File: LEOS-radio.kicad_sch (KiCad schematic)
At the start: 19 parts, among them J1 MicroFit_1x4, J2 MicroFit_1x4, U1 MCP2562FD, U2 MCP2518FD, Y1 40 MHz

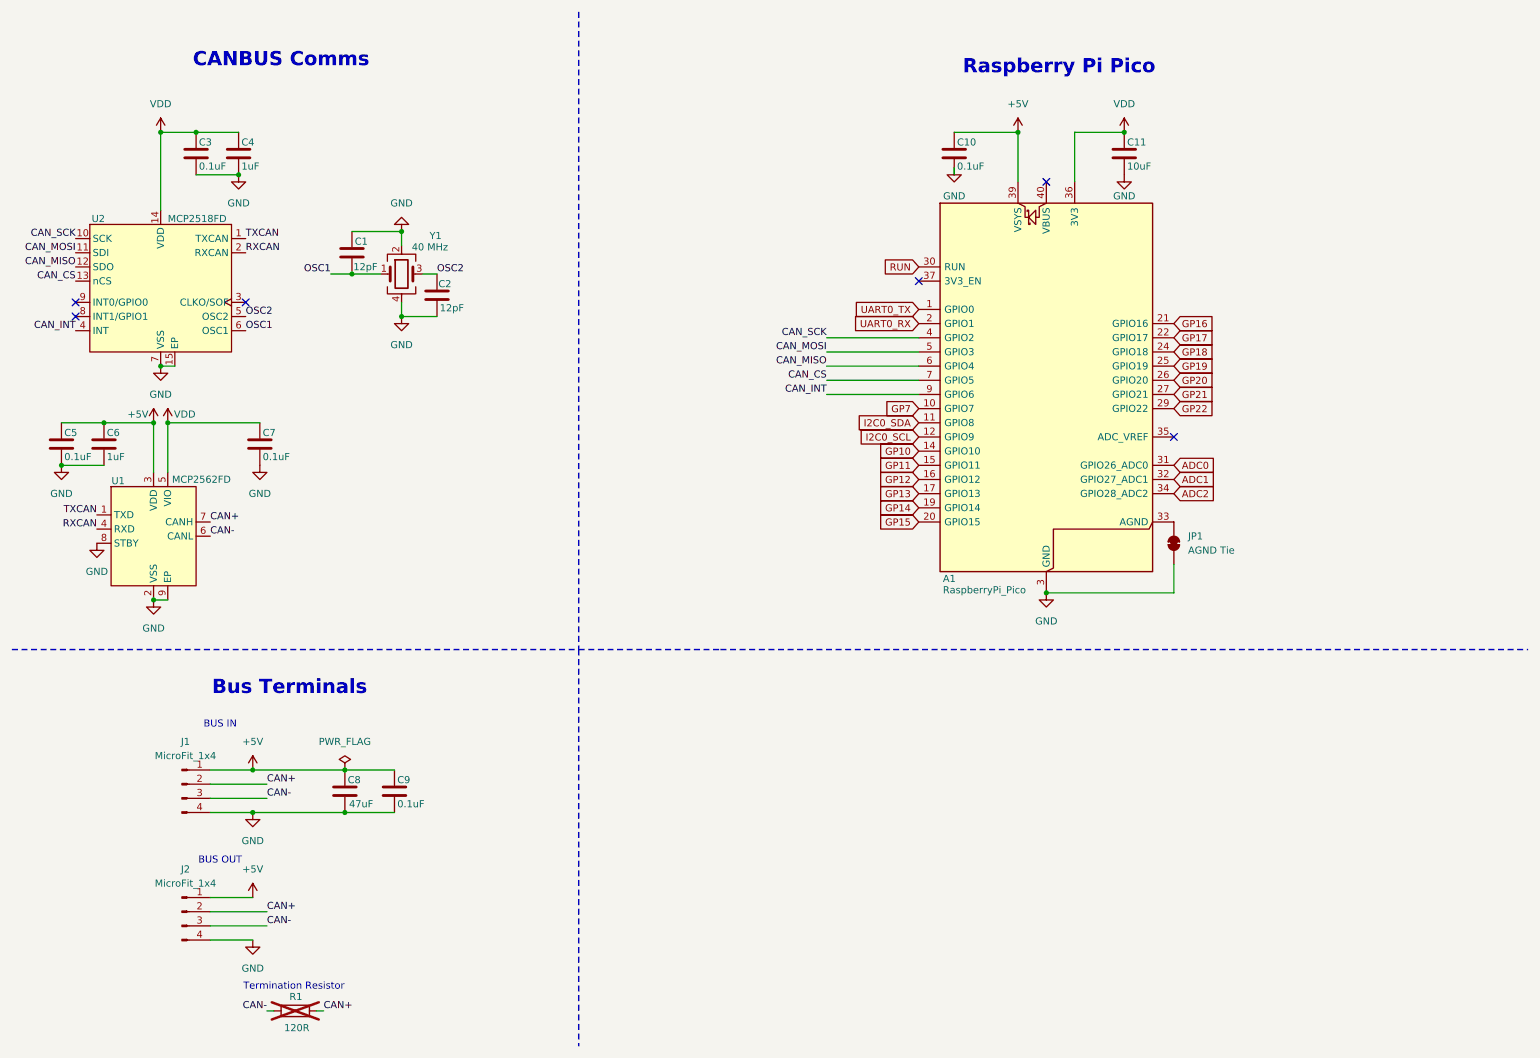
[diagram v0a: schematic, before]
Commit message: v2 with dual 1W LoRa transcievers, edge-mount SMA connectors, and an all new design
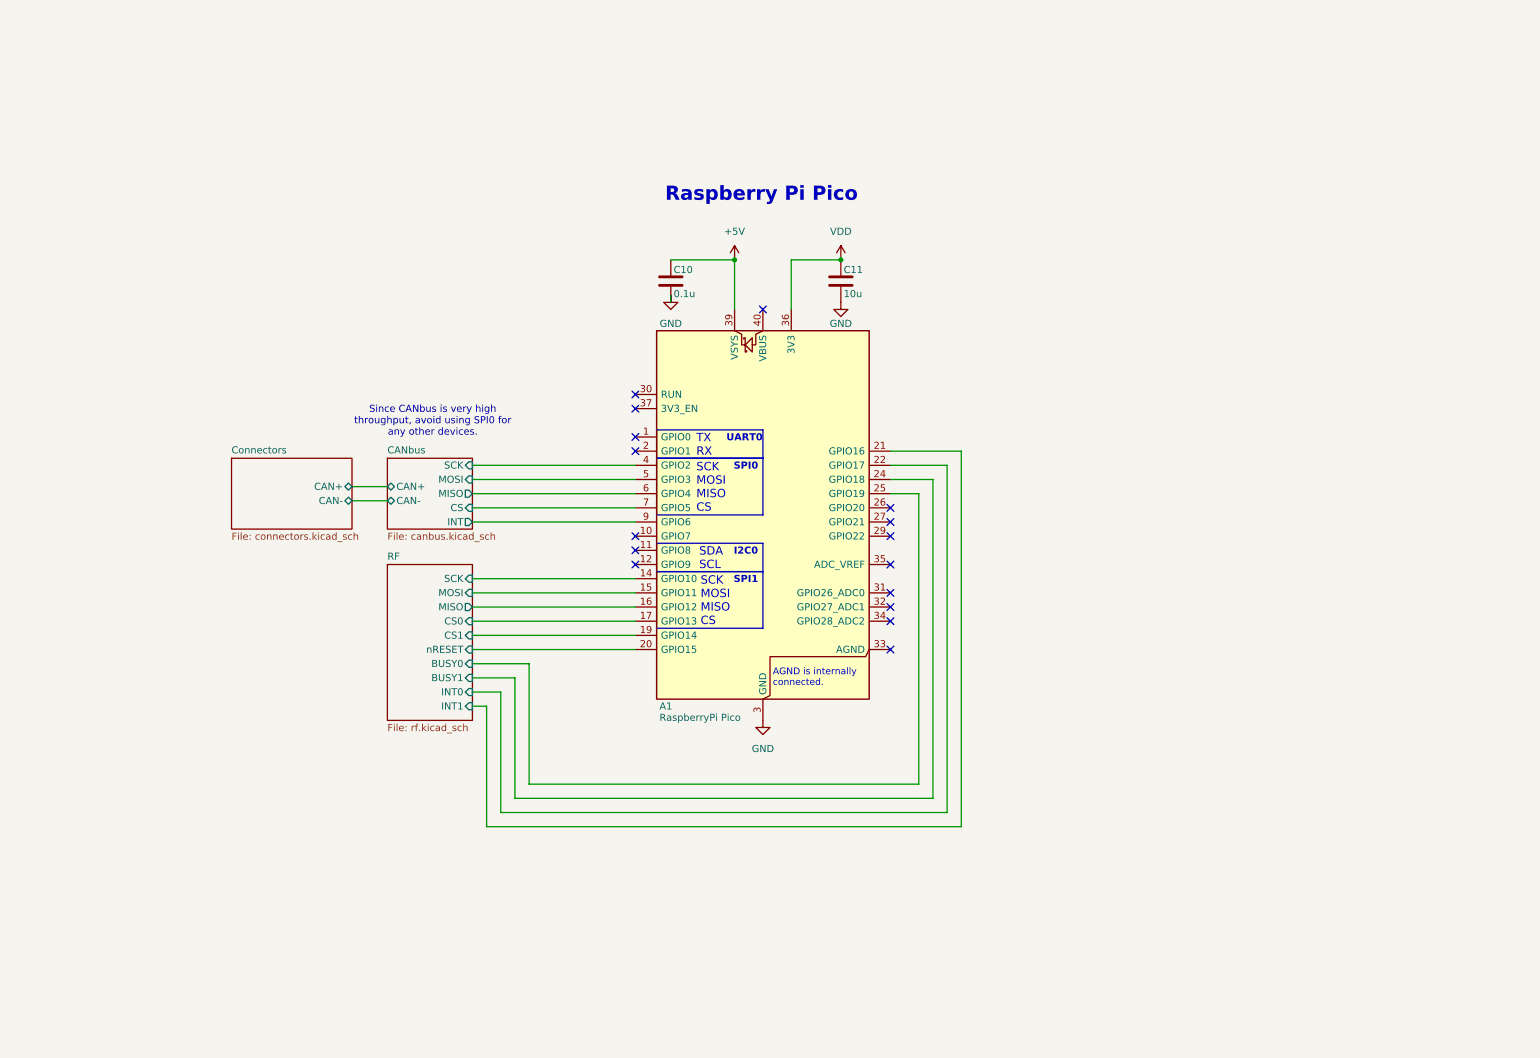
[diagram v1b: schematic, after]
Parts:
- removed C1, C2: 12pF, Capacitor_SMD:C_0603_1608Metric, symbol Device:C
- removed C3, C5, C7, C9: 0.1uF, Capacitor_SMD:C_0603_1608Metric, symbol Device:C
- removed C4, C6: 1uF, Capacitor_SMD:C_0603_1608Metric, symbol Device:C
- removed C8: 47uF, Capacitor_SMD:C_0603_1608Metric, symbol Device:C
- removed J1, J2: MicroFit_1x4, Connector_Molex:Molex_Micro-Fit_3.0_43650-0410_1x04-1MP_P3.00mm_Horizontal_PnP, symbol Connector:Conn_01x04_Pin
- removed JP1: AGND Tie, Jumper:SolderJumper-2_P1.3mm_Bridged_RoundedPad1.0x1.5mm, symbol Jumper:SolderJumper_2_Bridged
- removed R1: 120R, Resistor_THT:R_Axial_DIN0207_L6.3mm_D2.5mm_P7.62mm_Horizontal, symbol Device:R
- removed U1: MCP2562FD, Package_SO:SOIC-8_3.9x4.9mm_P1.27mm, symbol LEOS:MCP2562FD
- removed U2: MCP2518FD, Package_SO:SOIC-14_3.9x8.7mm_P1.27mm, symbol LEOS:MCP2518FD
- removed Y1: 40 MHz, Crystal:Crystal_SMD_3225-4Pin_3.2x2.5mm_HandSoldering, symbol Device:Crystal_GND24
- A1: value RaspberryPi_Pico -> RaspberryPi Pico; Digikey (none) -> 1778-PIM724-ND; MPN (none) -> PIM724; Manufacturer (none) -> Pimoroni
- C10: value 0.1uF -> 0.1u; Digikey (none) -> 1276-CL10B104KB8NNNLCT-ND; LCSC (none) -> C913912; MPN (none) -> CL10B104KB8NNNL; Manufacturer (none) -> Samsung Electro-Mechanics
- C11: value 10uF -> 10u; footprint Capacitor_SMD:C_0603_1608Metric -> Capacitor_SMD:C_0805_2012Metric; Digikey (none) -> 1276-2872-1-ND; LCSC (none) -> C95841; MPN (none) -> CL21B106KOQNNNE; Manufacturer (none) -> Samsung Electro-Mechanics
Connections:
- net ADC0: no longer names the net of A1.31 (GPIO26_ADC0)
- net ADC1: no longer names the net of A1.32 (GPIO27_ADC1)
- net ADC2: no longer names the net of A1.34 (GPIO28_ADC2)
- net CAN_CS renamed CANbus/CS
- net CAN_INT renamed CANbus/INT
- net CAN_MISO renamed CANbus/MISO
- net CAN_MOSI renamed CANbus/MOSI
- net CAN_SCK renamed CANbus/SCK
- net GP10 renamed RF/SCK
- net GP11 renamed RF/MOSI
- net GP12 renamed RF/MISO
- net GP13 renamed RF/CS0
- net GP14 renamed RF/CS1
- net GP15 renamed RF/nRESET
- net GP16 renamed RF/INT1
- net GP17 renamed RF/INT0
- net GP18 renamed RF/BUSY1
- net GP19 renamed RF/BUSY0
- net GP20: no longer names the net of A1.26 (GPIO20)
- net GP21: no longer names the net of A1.27 (GPIO21)
- net GP22: no longer names the net of A1.29 (GPIO22)
- net GP7: no longer names the net of A1.10 (GPIO7)
- net I2C0_SCL: no longer names the net of A1.12 (GPIO9)
- net I2C0_SDA: no longer names the net of A1.11 (GPIO8)
- net RUN: no longer names the net of A1.30 (RUN)
- net UART0_RX: no longer names the net of A1.2 (GPIO1)
- net UART0_TX: no longer names the net of A1.1 (GPIO0)
- no-connect marks 6 -> 16
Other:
- added sheet CANbus (canbus.kicad_sch)
- added sheet Connectors (connectors.kicad_sch)
- added sheet RF (rf.kicad_sch)
- note added: "AGND is internally connected."
- note added: "I2C0"
- note added: "SCK MOSI MISO CS"
- note added: "SDA SCL"
- note added: "SPI0"
- note added: "SPI1"
- note added: "Since CANbus is very high throughput, avoid using SPI0 for any other devices."
- note added: "TX RX"
- note added: "UART0"
- note removed: "BUS IN"
- note removed: "BUS OUT"
- note removed: "Bus Terminals"
- note removed: "CANBUS Comms"
- note removed: "Termination Resistor"
- title: LEOS Stack - Microcontroller & Connectivity -> LEOS Radio
- moved on the sheet: A1, C10, C11
